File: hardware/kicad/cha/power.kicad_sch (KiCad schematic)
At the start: 11 parts, among them J1 AES CHA, U1 AMS1117-3.3, U2 AP2112K-1.2

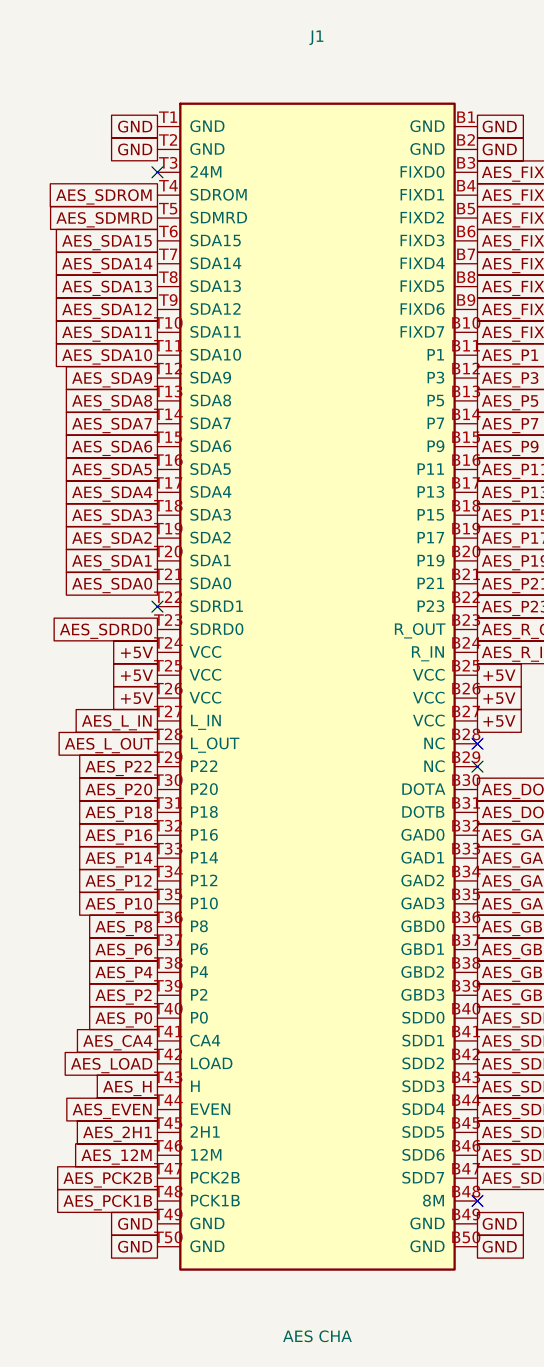
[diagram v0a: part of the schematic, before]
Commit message: Connecteur AES : numérotation officielle, empreinte et contours des cartes
Recoupement avec les cartes AES de jwestfall69 (neogeo-diag-aes-prog et
neogeo-diag-aes-cha, fabriquées et testées, domaine public) :
- la face « dessus » (contacts A, côté composants) était numérotée à
  l'envers : position n -> 51 - n. A1 et B1 sont à droite vus côté
  composants, l'un derrière l'autre (sérigraphie A1 des cartes NEO-AEG) ;
  face B inchangée. Les 200 contacts concordent désormais.
- empreinte : contacts 1,5 x 10 mm, centre à 7,1 mm du bord, T1 à droite.
- hardware/gen/outline.py : contours PROG (174 x 115 mm) et CHA
  (173 x 115 mm), languette 129,2 x 19 mm, encoches, trous de 10 mm et J1
  placé ; identiques aux cartes de référence à 0,01 mm près, recoupés
  sur la photo NEO-AEG PROG-EP du wiki.
Schémas, PDF, .pcf et documentation régénérés ; netlists identiques.

Co-Authored-By: Claude Opus 5.5 <noreply@anthropic.com>
Claude-Session: https://claude.ai/code/session_01WKfXP1YJ8otGxZ5dsY6Agh
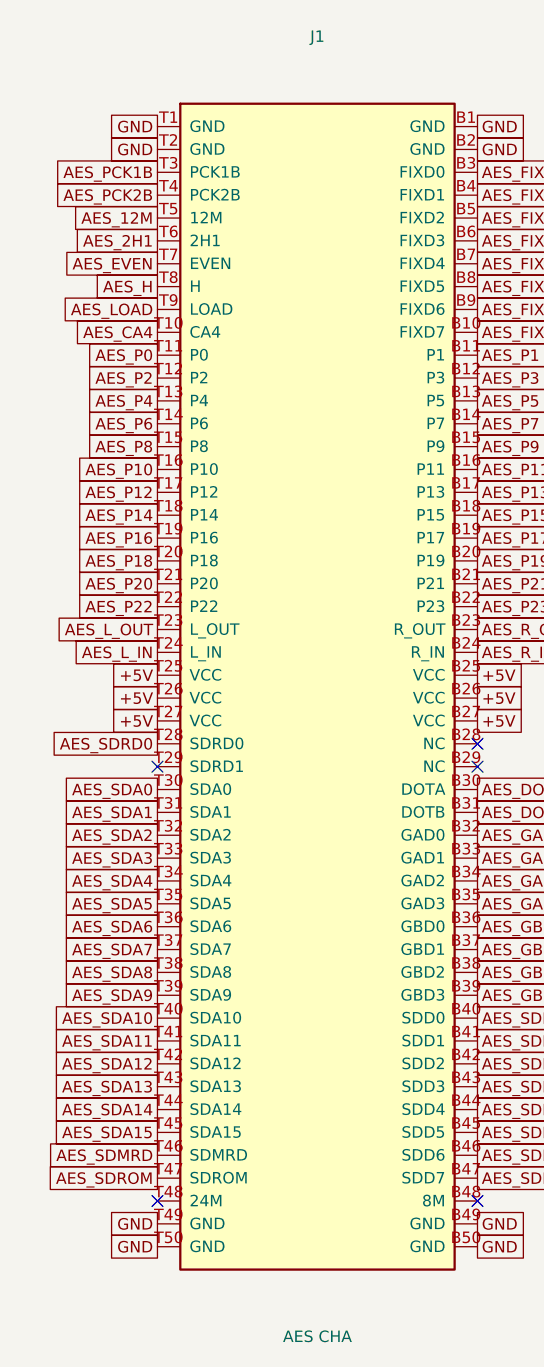
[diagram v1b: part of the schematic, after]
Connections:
- net +5V: now also J1.T27 (VCC); no longer J1.T24 (VCC)
- net AES_12M: now also J1.T5 (12M); no longer J1.T46 (12M)
- net AES_2H1: now also J1.T6 (2H1); no longer J1.T45 (2H1)
- net AES_CA4: now also J1.T10 (CA4); no longer J1.T41 (CA4)
- net AES_EVEN: now also J1.T7 (EVEN); no longer J1.T44 (EVEN)
- net AES_H: now also J1.T8 (H); no longer J1.T43 (H)
- net AES_LOAD: now also J1.T9 (LOAD); no longer J1.T42 (LOAD)
- net AES_L_IN: now also J1.T24 (L_IN); no longer J1.T27 (L_IN)
- net AES_L_OUT: now also J1.T23 (L_OUT); no longer J1.T28 (L_OUT)
- net AES_P0: now also J1.T11 (P0); no longer J1.T40 (P0)
- net AES_P10: now also J1.T16 (P10); no longer J1.T35 (P10)
- net AES_P12: now also J1.T17 (P12); no longer J1.T34 (P12)
- net AES_P14: now also J1.T18 (P14); no longer J1.T33 (P14)
- net AES_P16: now also J1.T19 (P16); no longer J1.T32 (P16)
- net AES_P18: now also J1.T20 (P18); no longer J1.T31 (P18)
- net AES_P2: now also J1.T12 (P2); no longer J1.T39 (P2)
- net AES_P20: now also J1.T21 (P20); no longer J1.T30 (P20)
- net AES_P22: now also J1.T22 (P22); no longer J1.T29 (P22)
- net AES_P4: now also J1.T13 (P4); no longer J1.T38 (P4)
- net AES_P6: now also J1.T14 (P6); no longer J1.T37 (P6)
- net AES_P8: now also J1.T15 (P8); no longer J1.T36 (P8)
- net AES_PCK1B: now also J1.T3 (PCK1B); no longer J1.T48 (PCK1B)
- net AES_PCK2B: now also J1.T4 (PCK2B); no longer J1.T47 (PCK2B)
- net AES_SDA0: now also J1.T30 (SDA0); no longer J1.T21 (SDA0)
- net AES_SDA1: now also J1.T31 (SDA1); no longer J1.T20 (SDA1)
- net AES_SDA10: now also J1.T40 (SDA10); no longer J1.T11 (SDA10)
- net AES_SDA11: now also J1.T41 (SDA11); no longer J1.T10 (SDA11)
- net AES_SDA12: now also J1.T42 (SDA12); no longer J1.T9 (SDA12)
- net AES_SDA13: now also J1.T43 (SDA13); no longer J1.T8 (SDA13)
- net AES_SDA14: now also J1.T44 (SDA14); no longer J1.T7 (SDA14)
- net AES_SDA15: now also J1.T45 (SDA15); no longer J1.T6 (SDA15)
- net AES_SDA2: now also J1.T32 (SDA2); no longer J1.T19 (SDA2)
- net AES_SDA3: now also J1.T33 (SDA3); no longer J1.T18 (SDA3)
- net AES_SDA4: now also J1.T34 (SDA4); no longer J1.T17 (SDA4)
- net AES_SDA5: now also J1.T35 (SDA5); no longer J1.T16 (SDA5)
- net AES_SDA6: now also J1.T36 (SDA6); no longer J1.T15 (SDA6)
- net AES_SDA7: now also J1.T37 (SDA7); no longer J1.T14 (SDA7)
- net AES_SDA8: now also J1.T38 (SDA8); no longer J1.T13 (SDA8)
- net AES_SDA9: now also J1.T39 (SDA9); no longer J1.T12 (SDA9)
- net AES_SDMRD: now also J1.T46 (SDMRD); no longer J1.T5 (SDMRD)
- net AES_SDRD0: now also J1.T28 (SDRD0); no longer J1.T23 (SDRD0)
- net AES_SDROM: now also J1.T47 (SDROM); no longer J1.T4 (SDROM)

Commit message: Régulateur 3,3 V à découpage, horloge SDRAM adaptée côté FPGA, U8 en 74AHCT125
- AP63203 (TSOT-23-6, sortie fixe 3,3 V, ~90 %) à la place de
  l'AMS1117 : ~0,15 W de pertes au lieu de ~0,75 W et moins de courant
  tiré sur le 5 V de la console ; L 4,7 µH, Cin 10 µF, Cout 2 x 22 µF.
- Résistance série de 33 ohms de l'horloge SDRAM déclarée avec le FPGA :
  placée à 2,7 mm de sa broche (au lieu de ~30 mm, côté SDRAM).
- CHA : U8 (16244 pour 2 canaux) remplacé par un 74AHCT125.
Cartes replacées, contrôle Freerouting sans violation ; routage des
deux cartes et vérification de timing en cours.

Co-Authored-By: Claude Opus 5.5 <noreply@anthropic.com>
Claude-Session: https://claude.ai/code/session_01WKfXP1YJ8otGxZ5dsY6Agh
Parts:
- removed U1: AMS1117-3.3, Package_TO_SOT_SMD:SOT-223-3_TabPin2, symbol Regulator_Linear:AMS1117-3.3
- added C7: 10u, Capacitor_SMD:C_0805_2012Metric, symbol Device:C
- added C8: 1u, Capacitor_SMD:C_0603_1608Metric, symbol Device:C
- added L1: 4,7 µH 3 A, Inductor_SMD:L_Bourns_SRP5030T, symbol Device:L
- added U1: AP63203WU, Package_TO_SOT_SMD:TSOT-23-6, symbol Regulator_Switching:AP63203WU
- C1: value 22u -> 10u; footprint Capacitor_SMD:C_1206_3216Metric -> Capacitor_SMD:C_0805_2012Metric
- C5: value 10u -> 22u; footprint Capacitor_SMD:C_0805_2012Metric -> Capacitor_SMD:C_1206_3216Metric
- C6: value 1u -> 22u; footprint Capacitor_SMD:C_0603_1608Metric -> Capacitor_SMD:C_1206_3216Metric
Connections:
- net +1V2: now also C7.1; no longer C5.1
- net +3V3: now also C5.1, C8.1, L1.2, U1.1 (FB); no longer C3.1, C4.1
- net +5V: now also C3.1, U1.2 (EN), U1.3 (IN)
- net GND: now also C7.2, C8.2, U1.4 (GND); no longer C4.2
- new net BST33: C4.1, U1.6 (BST)
- new net SW33: C4.2, L1.1, U1.5 (SW)
